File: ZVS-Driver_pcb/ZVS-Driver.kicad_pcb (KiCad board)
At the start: 2 copper layers, 22 parts, among them J1 Screw_Terminal_01x02, Q1 IRF540N, Q2 IRF540N, Q3 IRF540N, Q4 IRF540N, Q5 IRF540N

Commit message: new after presntation 15/3
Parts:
- moved C2 6.54 mm to (60.0, 105.5)
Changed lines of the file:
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@@
 	(footprint "Library:C_Radial_D10.0mm_H20.0mm_P4.5mm,customia"
 		(layer "F.Cu")
-		(at 64.75 110)
+		(at 60 105.5)
 		(descr "C, Radial series, Radial, pin pitch=5.00mm, diameter=10mm, height=20mm, Non-Polar Electrolytic Capacitor")
 		(tags "C Radial series Radial pin pitch 5.00mm diameter 10mm height 20mm Non-Polar Electrolytic Capacitor")

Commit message: Allages nikou
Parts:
- L2, L3: footprint Capacitor_THT:CP_Radial_D10.0mm_P5.00mm -> Inductor_THT:L_Radial_D10.0mm_P5.00mm_Fastron_07M
- moved C2 6.54 mm to (64.8, 110.0)
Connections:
- D6 pad 2: Net-(D4-K) -> Net-(D3-K)
- L3 pad 1: Net-(D3-K) -> Net-(D4-K)

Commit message: Routing
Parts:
- moved J1 108.9 mm to (131.9, 44.7)
- moved D4 98.8 mm to (111.2, 96.5), turned to -90 degrees
- moved Q3 84.0 mm to (103.8, 67.9), turned to -90 degrees
- moved Q4 82.9 mm to (103.8, 84.2), turned to -90 degrees
- moved Q5 75.4 mm to (95.8, 84.2), turned to -90 degrees
- moved R6 67.1 mm to (103.6, 60.5)
- moved R5 62.8 mm to (100.2, 109.2), turned to 90 degrees
- moved C2 48.1 mm to (108.5, 130.0), turned to 180 degrees
- moved L2 10.0 mm to (209.0, 81.0), turned to 90 degrees
- moved R1 7.67 mm to (149.3, 134.4), turned to 180 degrees
- moved Q2 4.23 mm to (185.8, 124.1)
- moved C1 3.10 mm to (224.4, 98.1)
- moved L1 1.60 mm to (142.4, 95.1)
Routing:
- net Net-(D1-A): track 0.00 -> 297.0 mm
- net 0: track 0.00 -> 273.0 mm
- net Net-(D3-K): track 0.00 -> 243.4 mm
- net Net-(D4-K): track 0.00 -> 243.0 mm
- net Net-(D4-A): track 0.00 -> 80.6 mm
- net Net-(D6-K): track 0.00 -> 62.1 mm
- net Net-(D1-K): track 0.00 -> 57.8 mm
- net Net-(Q3-D): track 0.00 -> 34.0 mm
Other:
- board outline added: 143.6 x 91.5 mm

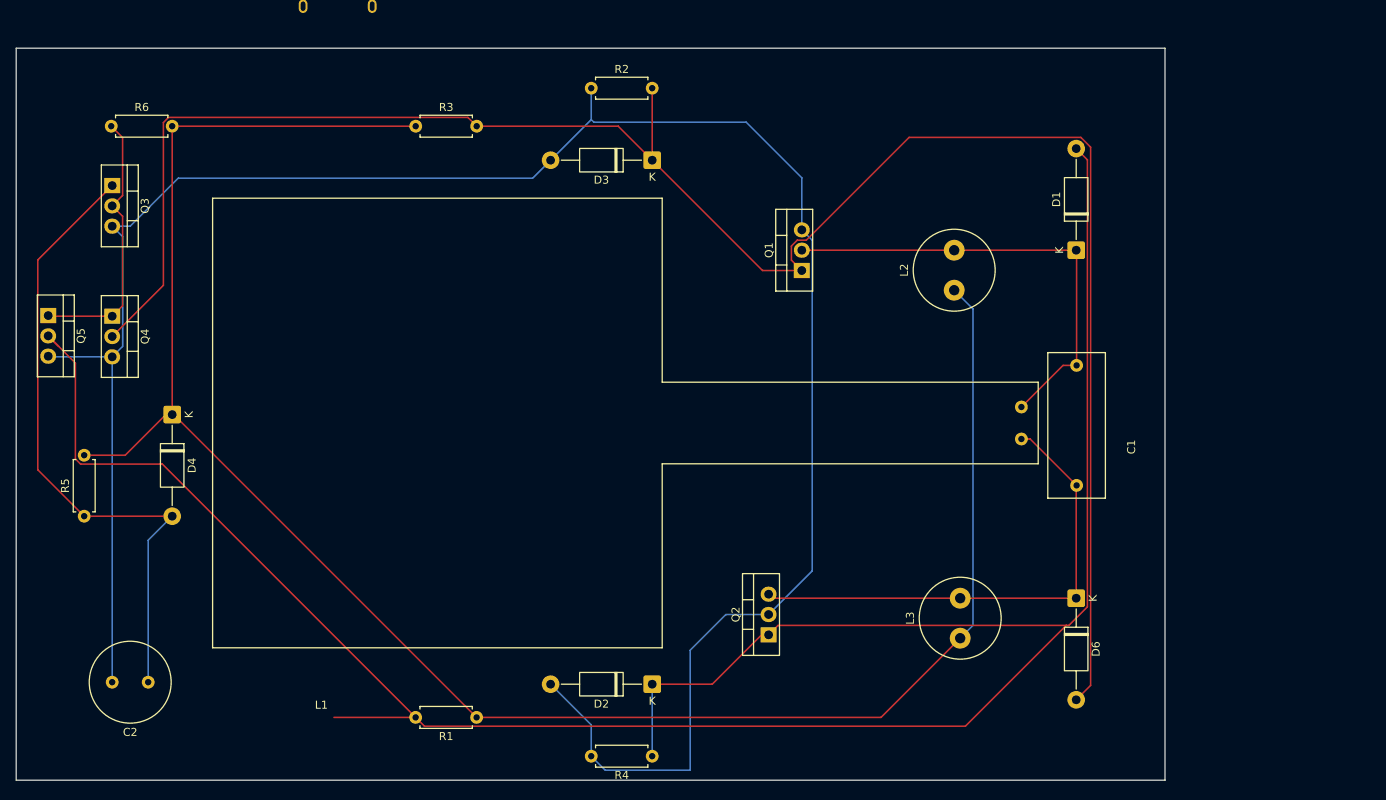
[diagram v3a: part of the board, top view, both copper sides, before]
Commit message: updated heatsinks and screw terminal as an input (havnet put the 4 usb c pins)
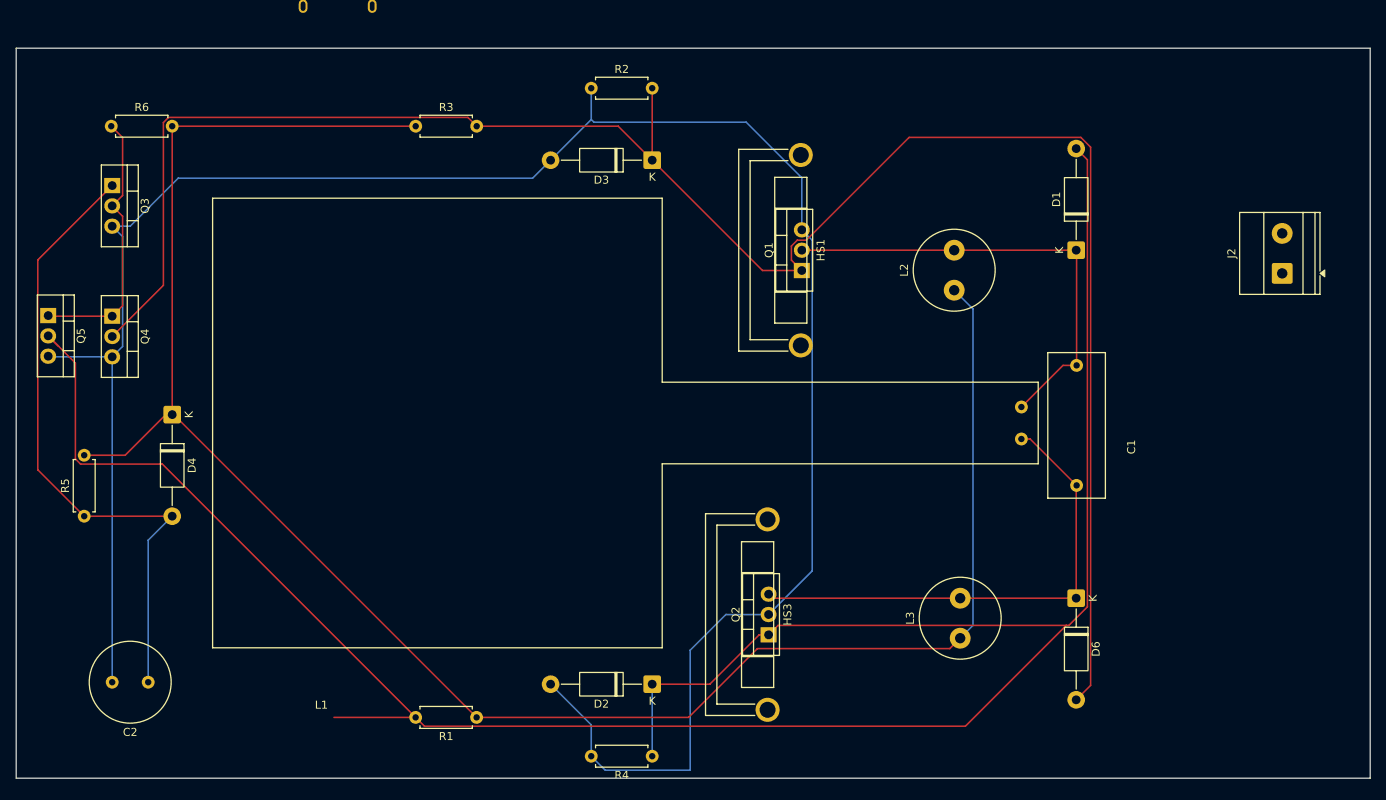
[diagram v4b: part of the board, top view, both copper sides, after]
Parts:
- added HS1: Heatsink, Heatsink:Heatsink_Fischer_FK224xx2201_25x8.3mm, F.Cu at (189.8, 64.1)
- added HS3: Heatsink, Heatsink:Heatsink_Fischer_FK224xx2201_25x8.3mm, F.Cu at (185.7, 109.7)
- added J2: Screw_Terminal_01x02, TerminalBlock_Phoenix:TerminalBlock_Phoenix_MKDS-1,5-2_1x02_P5.00mm_Horizontal, F.Cu at (250.0, 78.9)
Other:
- board size 143.6 x 91.5 mm -> 169.2 x 91.2 mm

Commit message: xwris to pinio sto kentro
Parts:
- moved J2 116.9 mm to (135.0, 58.0), turned to 0 degrees
- moved L1 106.3 mm to (248.7, 94.5), turned to 180 degrees
- moved R6 86.7 mm to (23.9, 94.6), turned to 90 degrees
- moved Q3 77.1 mm to (31.4, 94.5), turned to 0 degrees
- moved C1 65.5 mm to (159.1, 93.1)
- moved D1 65.5 mm to (158.9, 71.0)
- moved D6 65.5 mm to (158.9, 114.5)
- moved J1 65.5 mm to (66.6, 39.7)
- moved L2 65.5 mm to (143.7, 76.0)
- moved L3 65.5 mm to (144.4, 119.5)
- moved R1 65.5 mm to (84.0, 129.4)
- moved D2 65.5 mm to (106.0, 125.2)
- moved D3 65.5 mm to (106.0, 59.8)
- moved R2 65.5 mm to (98.3, 50.8)
- moved R3 65.5 mm to (76.4, 55.5)
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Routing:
- net Net-(D1-A): track 297.0 -> 181.7 mm
- net Net-(D4-K): track 243.0 -> 320.2 mm
- net 0: track 273.0 -> 246.4 mm
- net Net-(D6-K): track 62.1 -> 79.8 mm
- net Net-(Q3-D): track 34.0 -> 43.5 mm
- net Net-(D4-A): track 80.6 -> 87.4 mm
- net Net-(D3-K): track 243.4 -> 239.8 mm
- net Net-(D1-K): track 57.8 -> 56.9 mm
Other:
- board size 169.2 x 91.2 mm -> 157 x 96.2 mm
- board text added: "LC TANK"
- board text added: "SOFT START"

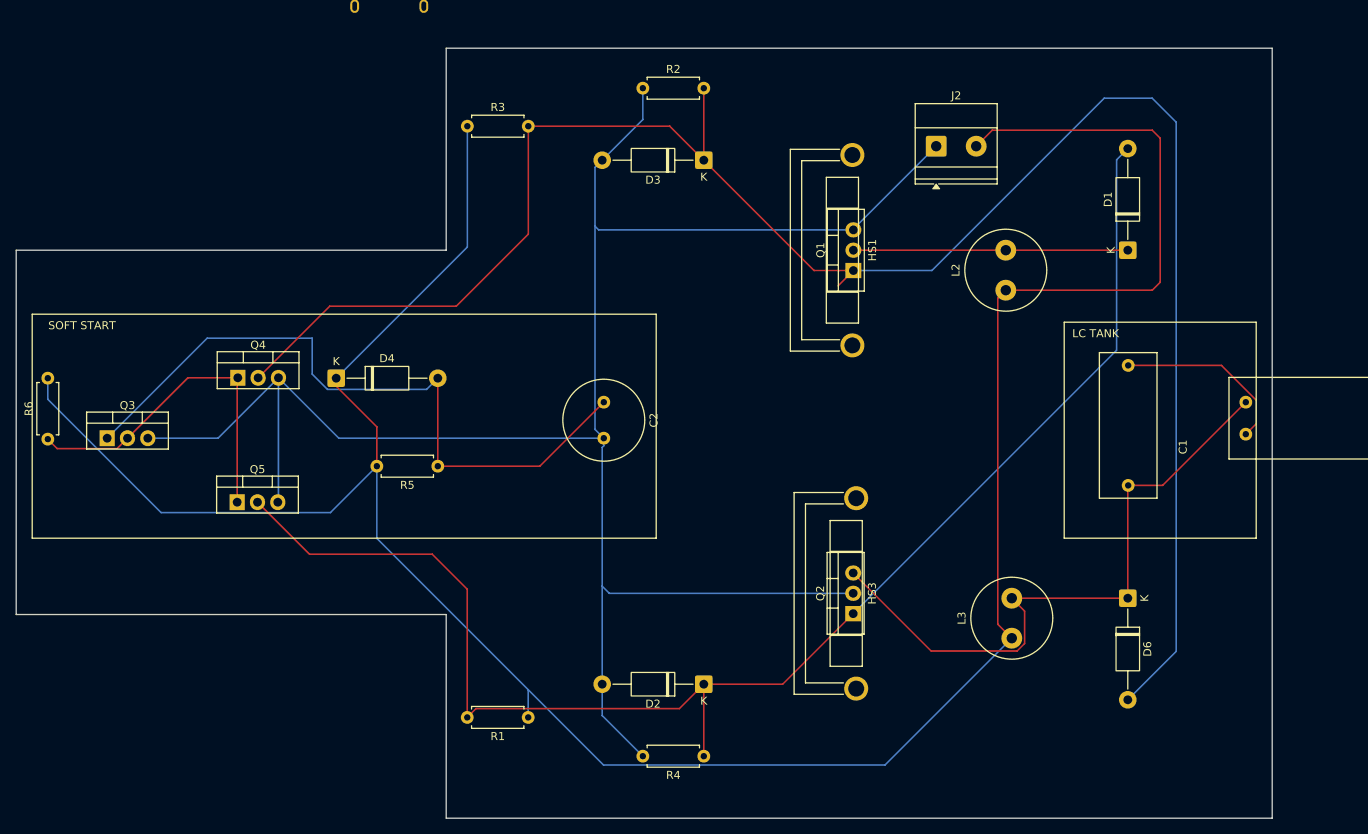
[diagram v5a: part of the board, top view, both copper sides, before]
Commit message: Pahos apo routes
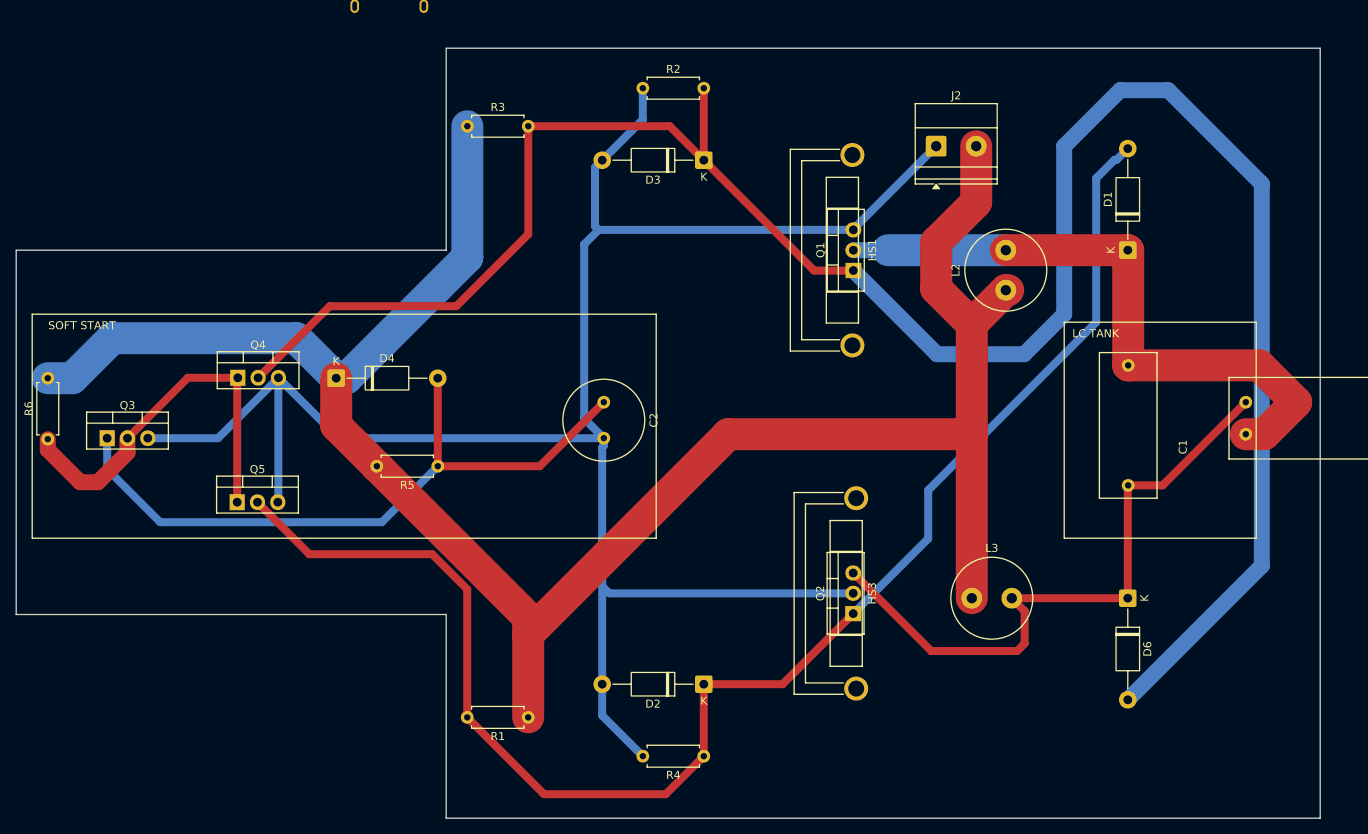
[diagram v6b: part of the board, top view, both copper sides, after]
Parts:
- moved L3 7.07 mm to (139.4, 114.5), turned to 0 degrees
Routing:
- net Net-(D4-K): track 320.2 -> 264.1 mm
- net Net-(D3-K): track 239.8 -> 269.5 mm
- net Net-(D1-K): track 56.9 -> 79.6 mm
- net Net-(Q3-D): track 43.5 -> 48.8 mm
- net Net-(D1-A): track 181.7 -> 186.1 mm
- net Net-(D4-A): track 87.4 -> 85.9 mm
- net 0: track 246.4 -> 247.3 mm
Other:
- board size 157 x 96.2 mm -> 163 x 96.2 mm

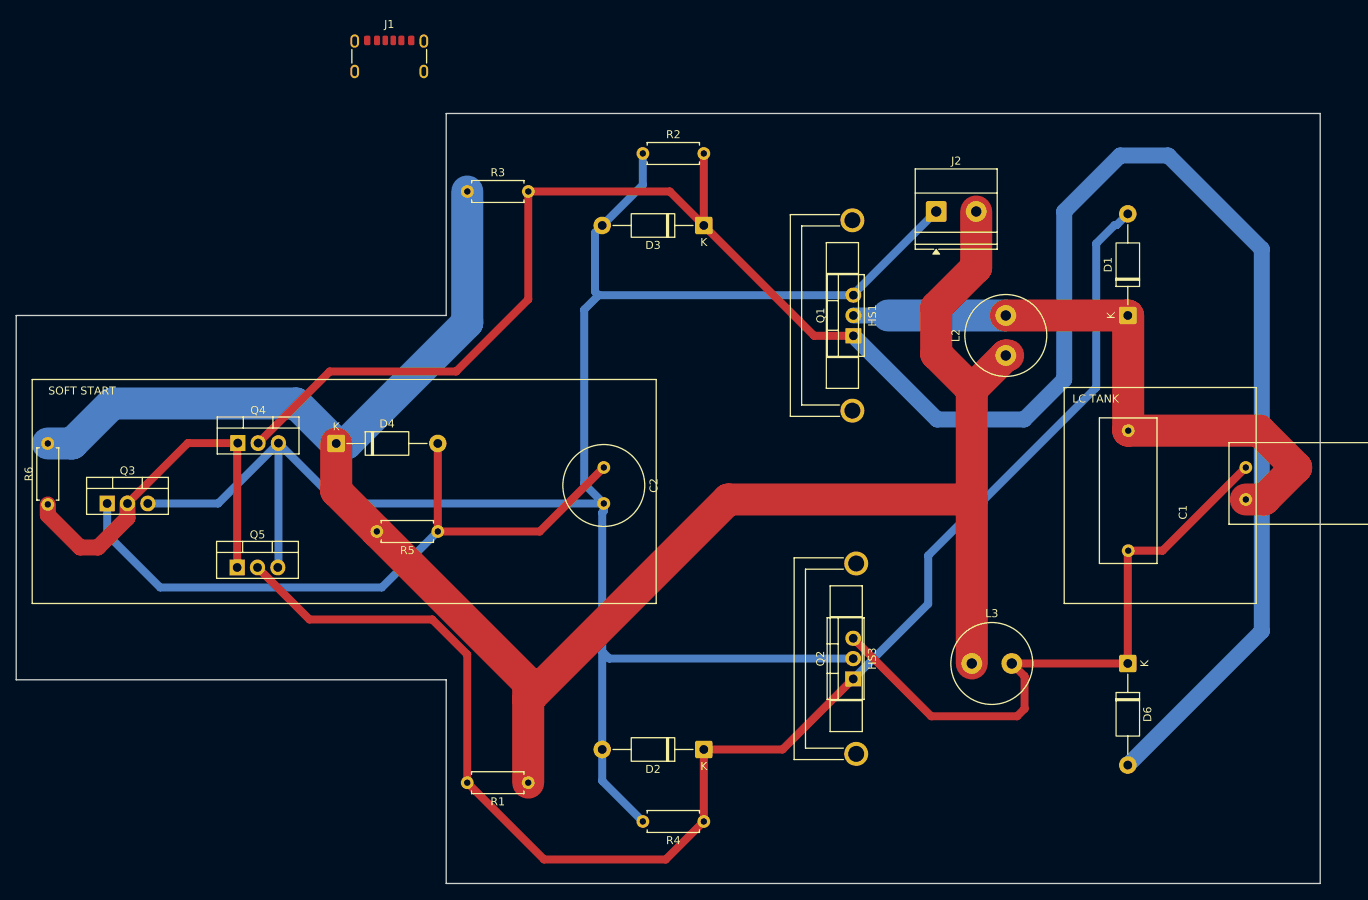
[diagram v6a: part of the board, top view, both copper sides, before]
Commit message: usb c eisodos kai routing stis eisodoys
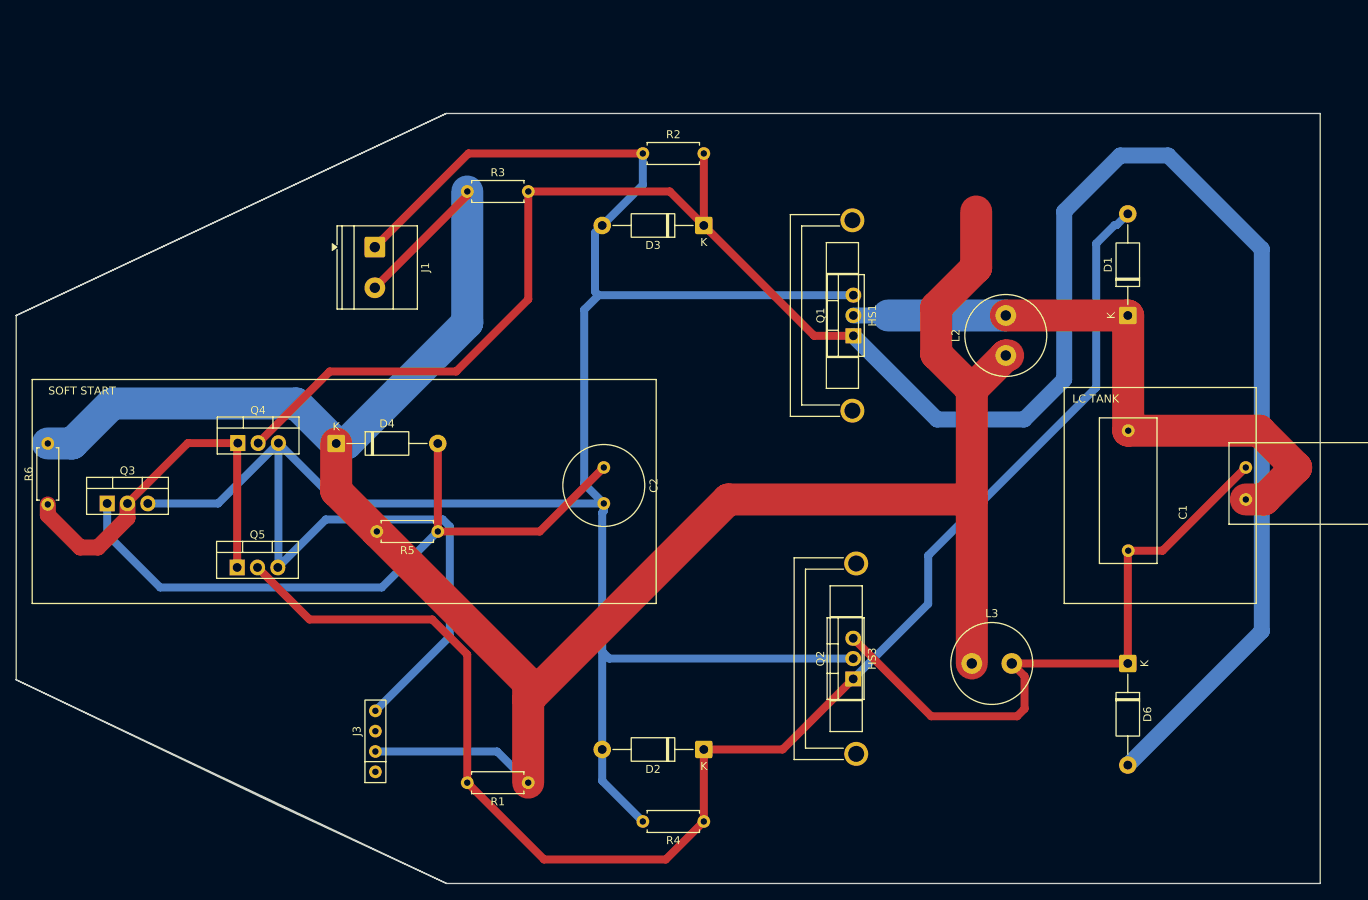
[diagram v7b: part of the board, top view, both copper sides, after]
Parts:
- removed J2: Screw_Terminal_01x02, TerminalBlock_Phoenix:TerminalBlock_Phoenix_MKDS-1,5-2_1x02_P5.00mm_Horizontal
- added J3: Screw_Terminal_01x04, usb_c_customia:usb_c_customia, F.Cu at (64.9, 128.0)
- J1: footprint Connector_USB:USB_C_Receptacle_GCT_USB4125-xx-x-0190_6P_TopMnt_Horizontal -> TerminalBlock_Phoenix:TerminalBlock_Phoenix_MKDS-1,5-2-5.08_1x02_P5.08mm_Horizontal
- moved J1 22.8 mm to (64.8, 62.5), turned to -90 degrees
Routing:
- net 0: track 247.3 -> 322.2 mm
- net Net-(D4-K): track 264.1 -> 301.6 mm
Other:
- outline, holes or cut-outs redrawn
